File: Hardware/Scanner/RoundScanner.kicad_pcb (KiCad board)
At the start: 4 copper layers, 45 x 42.5 mm, 83 parts, among them J1 I2C ThroughHole, J3 I2C, J4 Interface, Q1 BSS138DW-7-F, U1 OPA2376xxD, U2 NAU7802SGI, U4 OPA2376xxD, U5 TLC59208FIPWR, U6 AS7341-DLGT, U7 AP7312-1833W6-7, X1 SG-8002CE

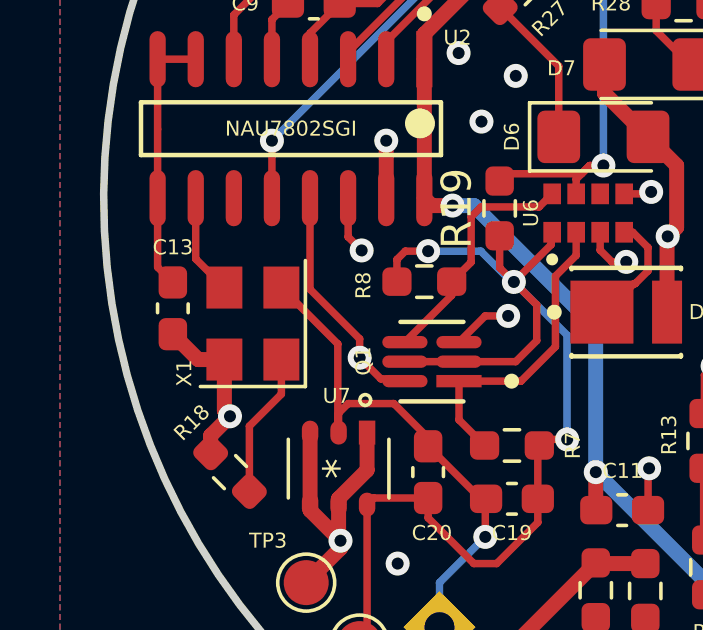
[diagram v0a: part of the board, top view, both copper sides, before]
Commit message: Updated LED and crystal descriptions
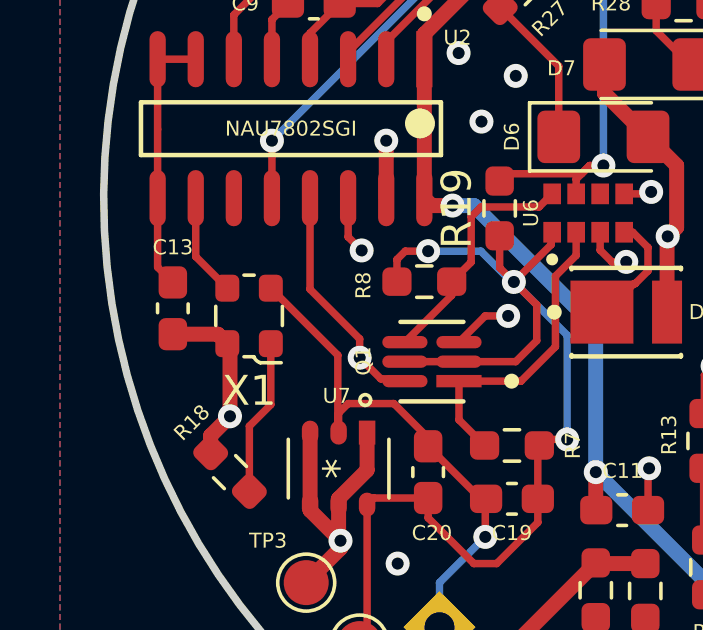
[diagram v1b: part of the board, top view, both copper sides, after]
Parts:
- D10: value LED -> 1650nm
- D11: value LED -> 1720nm
- D4: value LED -> 855nm
- D5: value LED -> 940nm
- D6: value LED -> 1050nm
- D7: value LED -> 1300nm
- D8: value LED -> 1460nm
- D9: value LED -> 1550nm
- X1: value SG-8002CE -> 4.9152 MHz; footprint Oscillator:Oscillator_SMD_SeikoEpson_SG8002CE-4Pin_3.2x2.5mm -> Oscillator:Oscillator_SMD_ECS_2520MV-xxx-xx-4Pin_2.5x2.0mm
- moved X1 0.28 mm to (71.6, 111.3), turned to 180 degrees

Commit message: Reestablish 3.3v zone fill on In2.CU
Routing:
- added copper zone on In2.Cu, net +3V3
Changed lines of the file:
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@@
+    )
+  )
+  (zone (net 8) (net_name "+3V3") (layer "In2.Cu") (hatch edge 0.508)
+    (connect_pads (clearance 0.8))
+    (min_thickness 0.254) (filled_areas_thickness no)
+    (fill yes (thermal_gap 0.508) (thermal_bridge_width 0.508))
+    (polygon
+      (pts
+        (xy 113.284 85.344)
+        (xy 112.903 131.699)
+        (xy 65.659 132.715)
+        (xy 65.659 85.217)
+      )
     )
   )

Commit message: LAtching circuit for controller board + minors
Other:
- board text added: "3.3v"
- board text added: "AS Int"
- board text added: "DRDY"
- board text added: "Gnd"
- board text added: "LEDreset"
- board text added: "SCL"
- board text added: "SDA"
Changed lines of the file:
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@@
     (effects (font (size 1 1) (thickness 0.15)) (justify mirror))
+  )
+  (gr_text "LEDreset\n" (at 101.981 97.79 45) (layer "B.SilkS")
+    (effects (font (size 0.5 0.5) (thickness 0.1)) (justify right mirror))
+  )
+  (gr_text "SDA" (at 82.804 124.206 45) (layer "B.SilkS")
+    (effects (font (size 1 1) (thickness 0.15)) (justify right mirror))
+  )
+  (gr_text "Gnd" (at 104.902 98.552 45) (layer "B.SilkS")
+    (effects (font (size 0.5 0.5) (thickness 0.1)) (justify right mirror))
+  )
+  (gr_text "SCL" (at 84.328 126.111 45) (layer "B.SilkS")
+    (effects (font (size 1 1) (thickness 0.15)) (justify right mirror))
+  )
+  (gr_text "AS Int" (at 100.584 95.377 45) (layer "B.SilkS")
+    (effects (font (size 0.5 0.5) (thickness 0.1)) (justify right mirror))
   )
   (gr_text "Power" (at 97.282 122.682) (layer "B.SilkS")
     (effects (font (size 1 1) (thickness 0.2)) (justify mirror))
   )
+  (gr_text "Gnd" (at 78.994 120.65 45) (layer "B.SilkS")
+    (effects (font (size 1 1) (thickness 0.15)) (justify right mirror))
+  )
+  (gr_text "DRDY" (at 99.314 90.424 45) (layer "B.SilkS")
+    (effects (font (size 0.5 0.5) (thickness 0.1)) (justify right mirror))
+  )
+  (gr_text "3.3v" (at 80.772 122.301 45) (layer "B.SilkS")
+    (effects (font (size 1 1) (thickness 0.15)) (justify right mirror))
+  )
   (segment (start 93.499808 121.285) (end 90.736663 121.285) (width 0.5) (layer "F.Cu") (net 1))

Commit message: Scanner & Controller Version 1.0
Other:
- board text added: "HandheldScanner v1.0 2022-12-23"
- board text removed: "HandheldScanner v0.8 2022-12-XX"
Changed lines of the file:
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@@
   (paper "A4")
   (title_block
-    (title "Plastic Scanner for AED")
-    (date "2022-06-07")
-    (rev "2")
+    (title "Scanner Module")
+    (date "2022-12-23")
+    (rev "1.0")
     (company "PlasticScanner")
     (comment 1 "By Markus Glavind")
+    (comment 4 "AISLER Project ID: UECHMLGI")
   )
   (layers
@@
   (gr_line (start 78.973236 87.335) (end 99.588764 87.335) (layer "Edge.Cuts") (width 0.25))
   (gr_arc (start 99.588764 87.335) (mid 89.281 129.835) (end 78.973236 87.335) (layer "Edge.Cuts") (width 0.25))
-  (gr_text "HandheldScanner v0.8\n2022-12-XX" (at 89.281 117.475) (layer "B.SilkS")
+  (gr_text "HandheldScanner v1.0\n2022-12-23" (at 89.281 117.475) (layer "B.SilkS")
     (effects (font (size 1 1) (thickness 0.15)) (justify mirror))
   )

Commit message: First commit - still a small error with compiling
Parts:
- removed C8, C9: 0.1uF, Capacitor_SMD:C_0603_1608Metric_Pad1.08x0.95mm_HandSolder
- removed R15, R17, R5, R6: 51, Resistor_SMD:R_0603_1608Metric_Pad0.98x0.95mm_HandSolder
- added JP1: Jumper_2_Bridged, Jumper:SolderJumper-2_P1.3mm_Bridged2Bar_RoundedPad1.0x1.5mm, F.Cu at (79.5, 103.8)
- C1, C11, C16, C18: value 100n -> 100nF
- C12, C2, C21, C3: value 51p -> 51pF
- C17: value 22u -> 22uF
- C22, C4: value 47n -> 47nF
- C23, C5: value 100p -> 100pF
- R26: value 62 -> 150
- R27: value 70 -> 240
- R28: value 75 -> 240
- R29, R30: value 75 -> 150
- R31: value 75 -> 40
- R32: value 82 -> 130
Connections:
- U2 pad 2: Net-(C8-Pad2) -> /ADC/AIN-
- U2 pad 3: Net-(C8-Pad1) -> /ADC/AIN+
- U2 pad 4: Net-(C9-Pad2) -> /ADC/AIN2-
- U2 pad 5: Net-(C9-Pad1) -> /ADC/AIN2+
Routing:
- net Net-(C8-Pad1): track 18.3 -> 0.00 mm, vias 2 -> 0
- net /ADC/AIN+: track 4.98 -> 21.5 mm, vias 0 -> 2
- net /ADC/AIN-: track 4.96 -> 17.8 mm
- net Net-(C9-Pad2): track 12.4 -> 0.00 mm
- net Net-(C8-Pad2): track 11.0 -> 0.00 mm
- net Net-(C9-Pad1): track 9.88 -> 0.00 mm
- net /ADC/AIN2+: track 50.6 -> 59.6 mm
- net /ADC/AIN2-: track 35.3 -> 43.1 mm
- net +2V5: track 66.1 -> 68.3 mm
- net +3V3: track 157.6 -> 159.5 mm, vias 11 -> 12
- net GND: vias 40 -> 37

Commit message: Firmware add
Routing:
- net Net-(C3-Pad1): track 22.1 -> 21.1 mm
- net Net-(R28-Pad1): track 27.2 -> 28.1 mm
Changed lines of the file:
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@@
   (segment (start 88.331 121.605) (end 88.331 121.769) (width 0.5) (layer "B.Cu") (net 1))
   (segment (start 90.424 92.71) (end 91.059 92.71) (width 0.5) (layer "B.Cu") (net 1))
-  (segment (start 90.7685 106.4768) (end 89.08048 104.78878) (width 0.25) (layer "F.Cu") (net 2))
-  (segment (start 94.800489 99.001511) (end 95.826511 97.975489) (width 0.25) (layer "F.Cu") (net 2))
-  (segment (start 97.65 95.377) (end 99.6515 95.377) (width 0.25) (layer "F.Cu") (net 2))
-  (segment (start 89.08048 100.78452) (end 90.863489 99.001511) (width 0.25) (layer "F.Cu") (net 2))
-  (segment (start 95.826511 96.751152) (end 97.200663 95.377) (width 0.25) (layer "F.Cu") (net 2))
-  (segment (start 95.826511 97.975489) (end 95.826511 96.751152) (width 0.25) (layer "F.Cu") (net 2))
-  (segment (start 89.08048 104.78878) (end 89.08048 100.78452) (width 0.25) (layer "F.Cu") (net 2))
-  (segment (start 100.006 95.0225) (end 101.734 95.0225) (width 0.25) (layer "F.Cu") (net 2))
-  (segment (start 90.863489 99.001511) (end 94.800489 99.001511) (width 0.25) (layer "F.Cu") (net 2))
-  (segment (start 99.6515 95.377) (end 100.006 95.0225) (width 0.25) (layer "F.Cu") (net 2))
+  (segment (start 97.65 95.377) (end 99.6515 95.377) (width 0.5) (layer "F.Cu") (net 2))
+  (segment (start 90.788971 99.126511) (end 94.725971 99.126511) (width 0.5) (layer "F.Cu") (net 2))
+  (segment (start 89.093511 100.821971) (end 90.788971 99.126511) (width 0.5) (layer "F.Cu") (net 2))
+  (segment (start 100.006 95.0225) (end 101.734 95.0225) (width 0.5) (layer "F.Cu") (net 2))
+  (segment (start 96.012 95.885) (end 96.52 95.377) (width 0.5) (layer "F.Cu") (net 2))
+  (segment (start 96.52 95.377) (end 97.200663 95.377) (width 0.5) (layer "F.Cu") (net 2))
+  (segment (start 96.012 97.840482) (end 96.012 95.885) (width 0.5) (layer "F.Cu") (net 2))
+  (segment (start 90.7685 106.4768) (end 89.093511 104.801811) (width 0.5) (layer "F.Cu") (net 2))
+  (segment (start 99.6515 95.377) (end 100.006 95.0225) (width 0.5) (layer "F.Cu") (net 2))
+  (segment (start 89.093511 104.801811) (end 89.093511 100.821971) (width 0.5) (layer "F.Cu") (net 2))
+  (segment (start 94.725971 99.126511) (end 96.012 97.840482) (width 0.5) (layer "F.Cu") (net 2))
   (segment (start 86.8915 91.567) (end 87.798799 91.567) (width 0.25) (layer "F.Cu") (net 3))
   (segment (start 102.8935 96.7975) (end 103.251 97.155) (width 0.25) (layer "F.Cu") (net 3))
@@
   (segment (start 88.0485 91.816701) (end 93.640799 97.409) (width 0.25) (layer "In1.Cu") (net 3))
   (segment (start 93.640799 97.409) (end 102.997 97.409) (width 0.25) (layer "In1.Cu") (net 3))
-  (segment (start 88.519 100.584) (end 90.551 98.552) (width 0.25) (layer "F.Cu") (net 4))
-  (segment (start 88.519 105.7513) (end 88.519 100.584) (width 0.25) (layer "F.Cu") (net 4))
-  (segment (start 88.576 93.8295) (end 90.304 93.8295) (width 0.25) (layer "F.Cu") (net 4))
-  (segment (start 90.551 98.552) (end 94.488 98.552) (width 0.25) (layer "F.Cu") (net 4))
-  (segment (start 92.71 94.107) (end 90.5815 94.107) (width 0.25) (layer "F.Cu") (net 4))
-  (segment (start 88.12052 106.14978) (end 88.519 105.7513) (width 0.25) (layer "F.Cu") (net 4))
-  (segment (start 95.377 96.324663) (end 93.159337 94.107) (width 0.25) (layer "F.Cu") (net 4))
-  (segment (start 94.488 98.552) (end 95.377 97.663) (width 0.25) (layer "F.Cu") (net 4))
-  (segment (start 95.377 97.663) (end 95.377 96.324663) (width 0.25) (layer "F.Cu") (net 4))
+  (segment (start 88.12052 106.14978) (end 88.265 106.0053) (width 0.5) (layer "F.Cu") (net 4))
+  (segment (start 88.576 93.8295) (end 90.304 93.8295) (width 0.5) (layer "F.Cu") (net 4))
+  (segment (start 94.234 95.181663) (end 93.159337 94.107) (width 0.5) (layer "F.Cu") (net 4))
+  (segment (start 92.71 94.107) (end 90.5815 94.107) (width 0.5) (layer "F.Cu") (net 4))
+  (segment (start 88.265 100.457) (end 90.424 98.298) (width 0.5) (layer "F.Cu") (net 4))
+  (segment (start 88.265 106.0053) (end 88.265 100.457) (width 0.5) (layer "F.Cu") (net 4))
+  (segment (start 90.424 98.298) (end 94.234 98.298) (width 0.5) (layer "F.Cu") (net 4))
+  (segment (start 94.234 98.298) (end 94.234 95.181663) (width 0.5) (layer "F.Cu") (net 4))
   (segment (start 87.757 93.366184) (end 88.413184 92.71) (width 0.25) (layer "F.Cu") (net 5))
   (segment (start 87.757 94.8355) (end 87.757 93.366184) (width 0.25) (layer "F.Cu") (net 5))
@@
   (segment (start 106.68 105.791) (end 93.753 105.791) (width 0.25) (layer "B.Cu") (net 21))
   (segment (start 93.753 105.791) (end 86.331 98.369) (width 0.25) (layer "B.Cu") (net 21))
-  (segment (start 88.646 98.933) (end 88.011 98.933) (width 0.25) (layer "F.Cu") (net 22))
   (segment (start 109.872 106.071) (end 108.357 106.071) (width 0.25) (layer "F.Cu") (net 22))
-  (segment (start 88.011 98.933) (end 87.0235 99.9205) (width 0.25) (layer "F.Cu") (net 22))
+  (segment (start 87.0235 99.2855) (end 88.011 98.298) (width 0.25) (layer "F.Cu") (net 22))
   (segment (start 108.357 106.071) (end 107.569 105.283) (width 0.25) (layer "F.Cu") (net 22))
-  (segment (start 87.0235 100.889) (end 87.0235 99.9205) (width 0.25) (layer "F.Cu") (net 22))
+  (segment (start 87.0235 100.889) (end 87.0235 99.2855) (width 0.25) (layer "F.Cu") (net 22))
   (via (at 107.569 105.283) (size 0.8) (drill 0.4) (layers "F.Cu" "B.Cu") (net 22))
-  (via (at 88.646 98.933) (size 0.8) (drill 0.4) (layers "F.Cu" "B.Cu") (net 22))
-  (segment (start 94.756501 105.043501) (end 88.646 98.933) (width 0.25) (layer "B.Cu") (net 22))
+  (via (at 88.011 98.298) (size 0.8) (drill 0.4) (layers "F.Cu" "B.Cu") (net 22))
+  (segment (start 107.569 105.283) (end 107.329501 105.043501) (width 0.25) (layer "B.Cu") (net 22))
   (segment (start 107.329501 105.043501) (end 94.756501 105.043501) (width 0.25) (layer "B.Cu") (net 22))
-  (segment (start 107.569 105.283) (end 107.329501 105.043501) (width 0.25) (layer "B.Cu") (net 22))
+  (segment (start 94.756501 105.043501) (end 88.011 98.298) (width 0.25) (layer "B.Cu") (net 22))
   (segment (start 103.996 105.421) (end 103.996 102.599) (width 0.25) (layer "F.Cu") (net 23))
   (segment (start 103.996 102.599) (end 103.515235 102.118235) (width 0.25) (layer "F.Cu") (net 23))
@@
   (segment (start 90.7431 108.7374) (end 88.58051 110.89999) (width 0.25) (layer "F.Cu") (net 37))
   (segment (start 92.630511 118.132807) (end 92.630511 118.688185) (width 0.25) (layer "F.Cu") (net 37))
-  (segment (start 88.58051 115.86851) (end 89.831489 117.119489) (width 0.25) (layer "F.Cu") (net 37))
+  (segment (start 88.58051 115.86851) (end 89.831489 117.119489) (width 0.5) (layer "F.Cu") (net 37))
   (segment (start 95.676663 120.015) (end 97.297163 120.015) (width 0.25) (layer "F.Cu") (net 38))
   (segment (start 100.930163 120.65) (end 99.763663 119.4835) (width 0.25) (layer "F.Cu") (net 38))
@@
   (via (at 108.839 99.568) (size 0.8) (drill 0.4) (layers "F.Cu" "B.Cu") (free) (net 43))
   (via (at 99.06 107.823) (size 0.8) (drill 0.4) (layers "F.Cu" "B.Cu") (free) (net 43))
-  (via (at 103.378 98.806) (size 0.8) (drill 0.4) (layers "F.Cu" "B.Cu") (free) (net 43))
+  (via (at 103.378 98.854011) (size 0.8) (drill 0.4) (layers "F.Cu" "B.Cu") (free) (net 43))
   (via (at 97.028 102.489) (size 0.8) (drill 0.4) (layers "F.Cu" "B.Cu") (free) (net 43))
   (via (at 84.328 88.773) (size 0.8) (drill 0.4) (layers "F.Cu" "B.Cu") (free) (net 43))
